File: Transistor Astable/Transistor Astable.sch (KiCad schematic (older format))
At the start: 12 parts, among them Q1 2N3904, Q2 2N3904

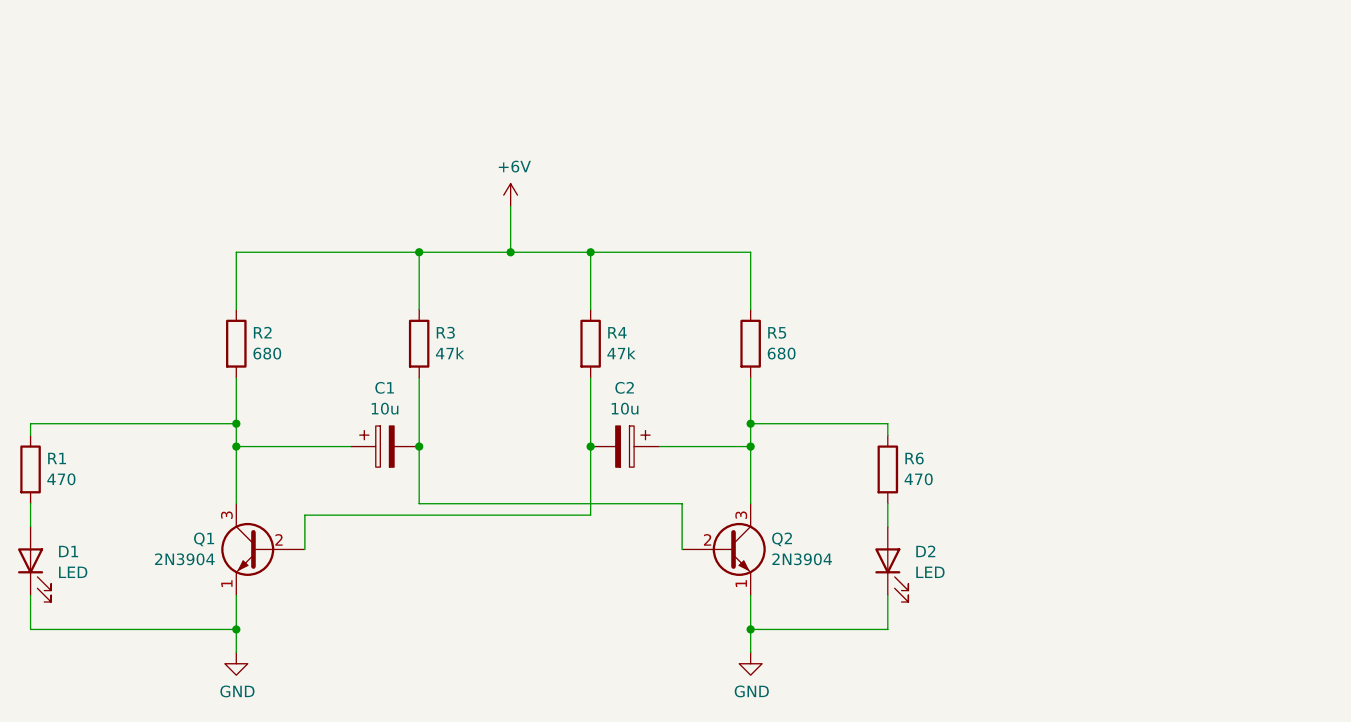
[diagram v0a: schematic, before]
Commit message: Change to PNP
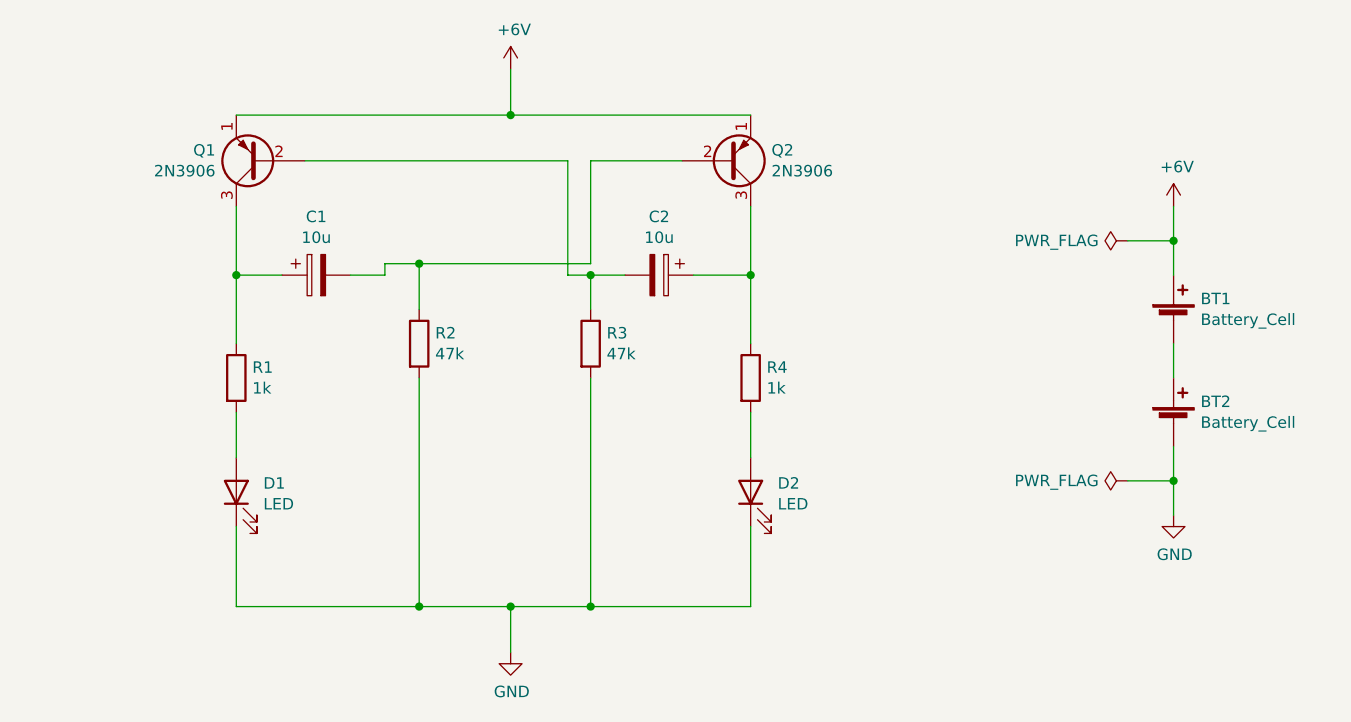
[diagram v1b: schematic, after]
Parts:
- removed Q1, Q2: 2N3904, Package_TO_SOT_THT:TO-92_Inline_Wide, symbol Transistor_BJT:2N3904
- removed R1, R6: 470, Resistor_THT:R_Axial_DIN0207_L6.3mm_D2.5mm_P7.62mm_Horizontal, symbol Device:R
- added BT1, BT2: Battery_Cell, symbol Device:Battery_Cell
- added Q1, Q2: 2N3906, Package_TO_SOT_THT:TO-92_Inline_Wide, symbol Transistor_BJT:2N3906
- R1: renamed from R2; value 680 -> 1k
- R4: renamed from R5; value 680 -> 1k
- renumbered R3 to R2, R4 to R3
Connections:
- net +6V: now also BT1.1 (+), Q1.1 (E), Q2.1 (E); no longer R1.1, R2.1, R3.1, R4.1
- net GND: now also R2.2, R3.2, BT2.2 (-)
- net at C1.2: now also R2.1, Q2.2 (B); no longer R2.2
- net at C2.1: now also R4.1, Q2.3 (C); no longer R4.2
- net at C2.2: now also R3.1, Q1.2 (B); no longer R3.2
- net at C1.1: now also R1.1, Q1.3 (C); no longer R1.2
- net at D1.2 (A): now also R1.2
- net at D2.2 (A): now also R4.2
- new net: BT1.2 (-), BT2.1 (+)
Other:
- moved on the sheet: C1, C2, D1, D2, R1, R4

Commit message: Adding footprint and initial routing
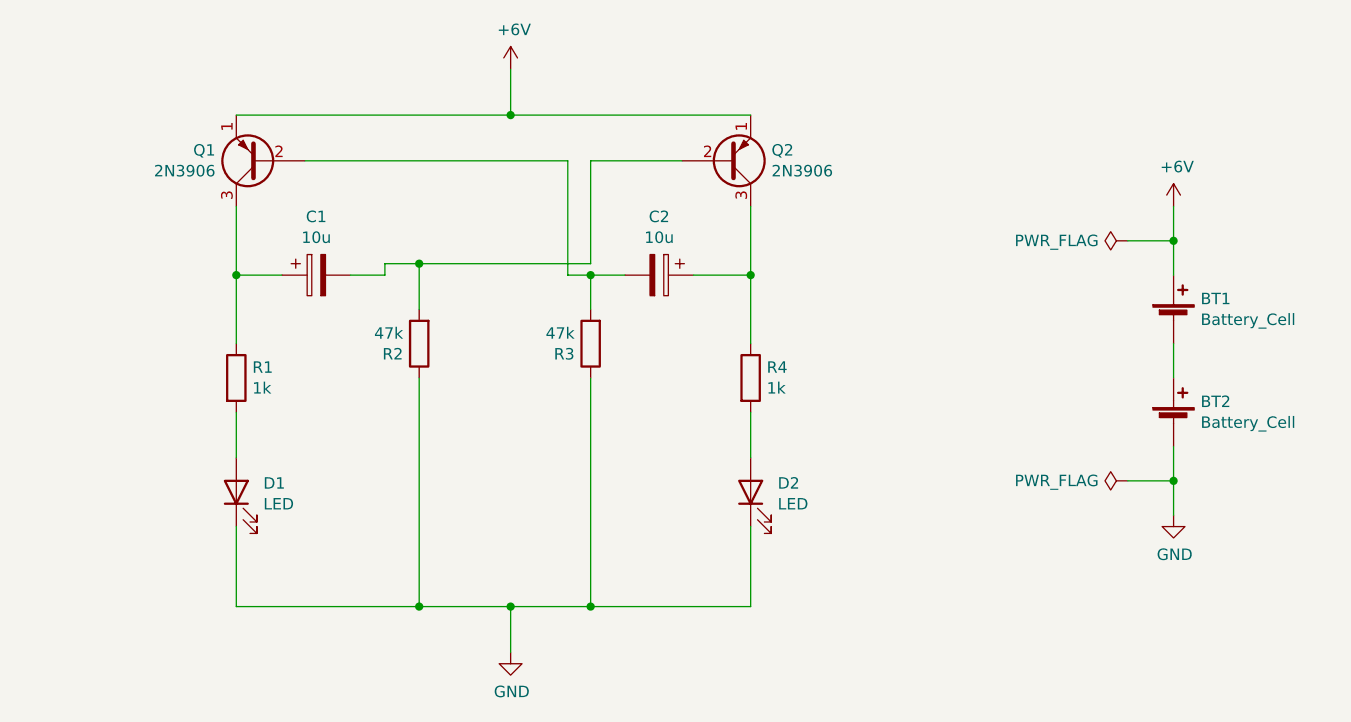
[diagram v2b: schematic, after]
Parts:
- BT1, BT2: footprint (none) -> Transistor Astable:BattHold_Linx_CR2032
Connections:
- net GND: now also R2.1, R3.1; no longer R2.2, R3.2
- net at C2.2, Q1.2 (B): now also R3.2; no longer R3.1
- net at C1.2, Q2.2 (B): now also R2.2; no longer R2.1
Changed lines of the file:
@@
 F 3 "~" H 5950 3100 50  0001 C CNN
 	1    5950 3100
-	1    0    0    -1
+	-1   0    0    1
 $EndComp
 $Comp
@@
 F 3 "~" H 6700 3100 50  0001 C CNN
 	1    6700 3100
-	1    0    0    -1
+	-1   0    0    1
 $EndComp
 $Comp
@@
 F 0 "BT1" H 9368 3096 50  0000 L CNN
 F 1 "Battery_Cell" H 9368 3005 50  0000 L CNN
-F 2 "" V 9250 3060 50  0001 C CNN
+F 2 "Transistor Astable:BattHold_Linx_CR2032" V 9250 3060 50  0001 C CNN
 F 3 "~" V 9250 3060 50  0001 C CNN
 	1    9250 3000
@@
 F 0 "BT2" H 9368 3546 50  0000 L CNN
 F 1 "Battery_Cell" H 9368 3455 50  0000 L CNN
-F 2 "" V 9250 3510 50  0001 C CNN
+F 2 "Transistor Astable:BattHold_Linx_CR2032" V 9250 3510 50  0001 C CNN
 F 3 "~" V 9250 3510 50  0001 C CNN
 	1    9250 3450
